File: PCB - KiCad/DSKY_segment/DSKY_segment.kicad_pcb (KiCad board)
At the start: 2 copper layers, 62.4 x 105.7 mm, 5 parts, among them J1 Conn_15X4, J2 Conn_15X4, J3 Conn_15X4

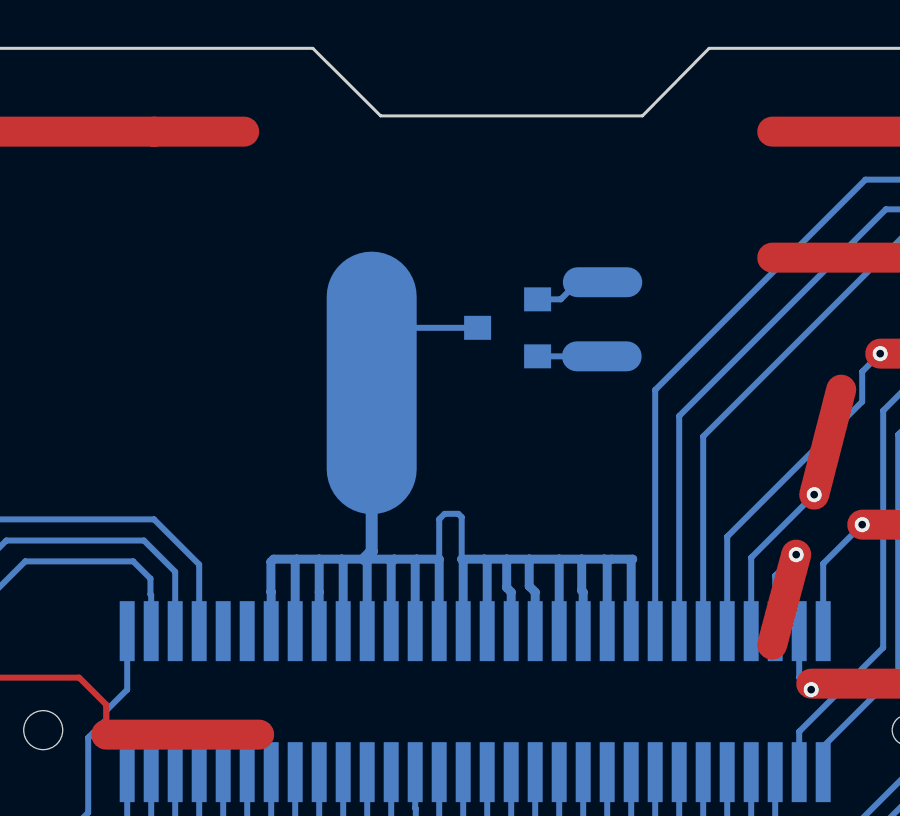
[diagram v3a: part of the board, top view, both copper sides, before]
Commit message: Add 0402 size current limiting resistors. Update PCB markings
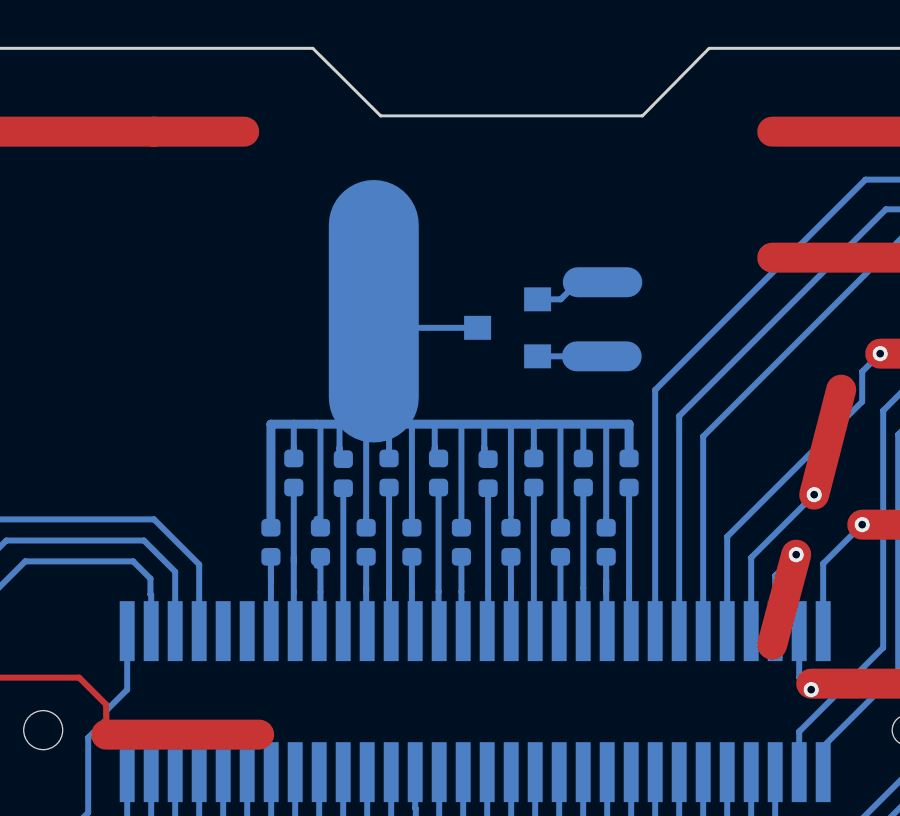
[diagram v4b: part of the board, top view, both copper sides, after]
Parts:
- added R1: 47K, Resistor_SMD:R_0402_1005Metric, B.Cu at (143.9, 43.7)
- added R10: 47K, Resistor_SMD:R_0402_1005Metric, B.Cu at (151.1, 41.4)
- added R11: 47K, Resistor_SMD:R_0402_1005Metric, B.Cu at (151.9, 43.7)
- added R12: 47K, Resistor_SMD:R_0402_1005Metric, B.Cu at (152.7, 41.4)
- added R13: 47K, Resistor_SMD:R_0402_1005Metric, B.Cu at (153.5, 43.7)
- added R14: 47K, Resistor_SMD:R_0402_1005Metric, B.Cu at (154.3, 41.4)
- added R15: 47K, Resistor_SMD:R_0402_1005Metric, B.Cu at (155.1, 43.7)
- added R16: 47K, Resistor_SMD:R_0402_1005Metric, B.Cu at (155.8, 41.4)
- added R2: 47K, Resistor_SMD:R_0402_1005Metric, B.Cu at (144.7, 41.4)
- added R3: 47K, Resistor_SMD:R_0402_1005Metric, B.Cu at (145.5, 43.7)
- added R4: 47K, Resistor_SMD:R_0402_1005Metric, B.Cu at (146.3, 41.4)
- added R5: 47K, Resistor_SMD:R_0402_1005Metric, B.Cu at (147.1, 43.7)
- added R6: 47K, Resistor_SMD:R_0402_1005Metric, B.Cu at (147.8, 41.4)
- added R7: 47K, Resistor_SMD:R_0402_1005Metric, B.Cu at (148.6, 43.7)
- added R8: 47K, Resistor_SMD:R_0402_1005Metric, B.Cu at (149.5, 41.4)
- added R9: 47K, Resistor_SMD:R_0402_1005Metric, B.Cu at (150.2, 43.7)
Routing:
- net Net-(D1-Pad3): track 3.96 -> 63.1 mm
- net (no net): track 3871.3 -> 3815.9 mm
- net Net-(R6-Pad2): track 0.00 -> 4.36 mm
- net Net-(R16-Pad2): track 0.00 -> 4.24 mm
- net Net-(R14-Pad2): track 0.00 -> 4.24 mm
- net Net-(R12-Pad2): track 0.00 -> 4.16 mm
- net Net-(R4-Pad2): track 0.00 -> 4.11 mm
- net Net-(R8-Pad2): track 0.00 -> 3.19 mm
- net Net-(R10-Pad2): track 0.00 -> 3.18 mm
- net Net-(R15-Pad2): track 0.00 -> 2.86 mm
- net Net-(R1-Pad2): track 0.00 -> 2.59 mm
- net Net-(R13-Pad2): track 0.00 -> 2.23 mm
- net Net-(R5-Pad2): track 0.00 -> 2.19 mm
- net Net-(R7-Pad2): track 0.00 -> 1.93 mm
- net Net-(R11-Pad2): track 0.00 -> 1.93 mm
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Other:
- board text added: "070720"
- board text added: "DSKY_V5_SEG"
- board text removed: "050519"
- board text removed: "DSKY_V4_SEG"
